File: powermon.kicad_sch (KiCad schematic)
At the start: 3 parts

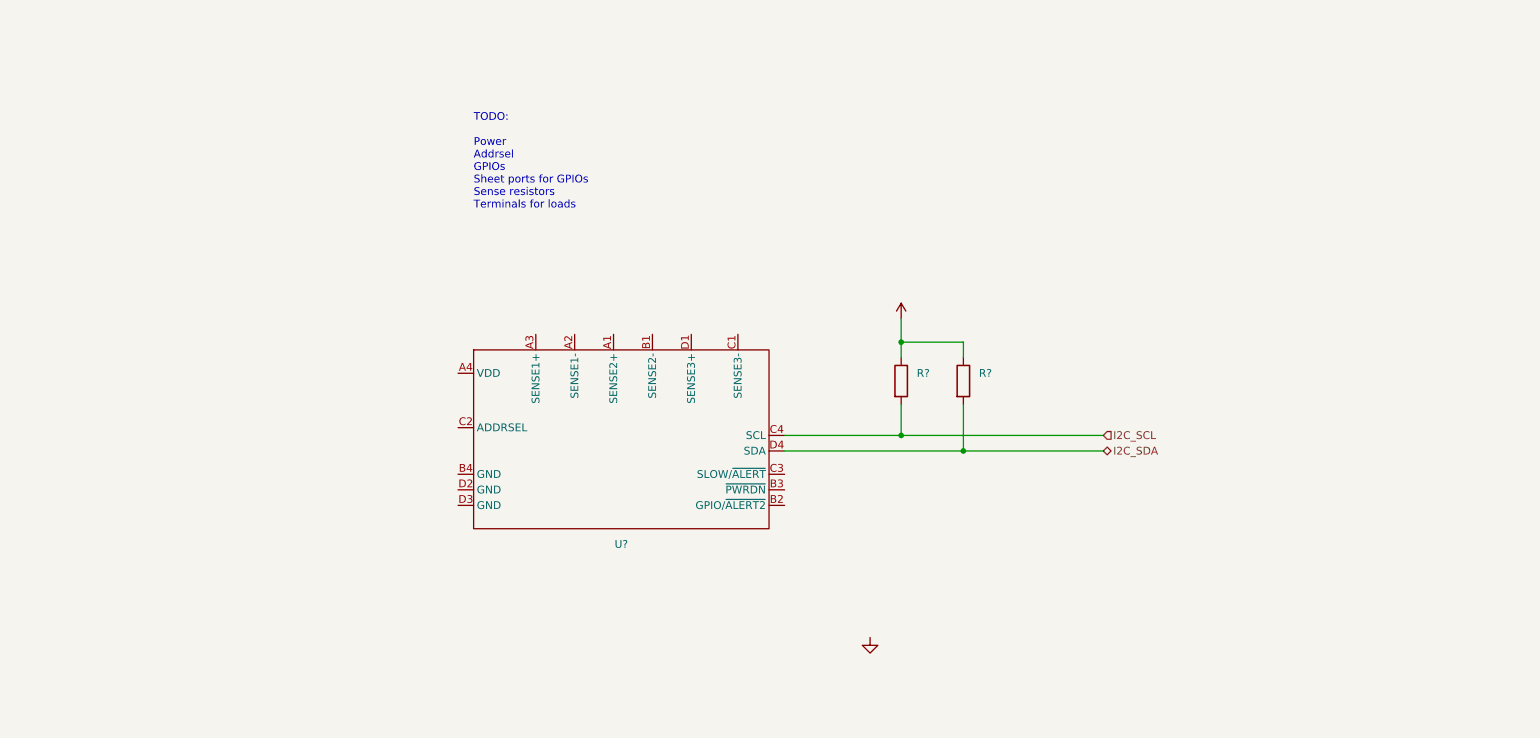
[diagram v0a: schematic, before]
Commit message: WiP: PAC1953 power monitor
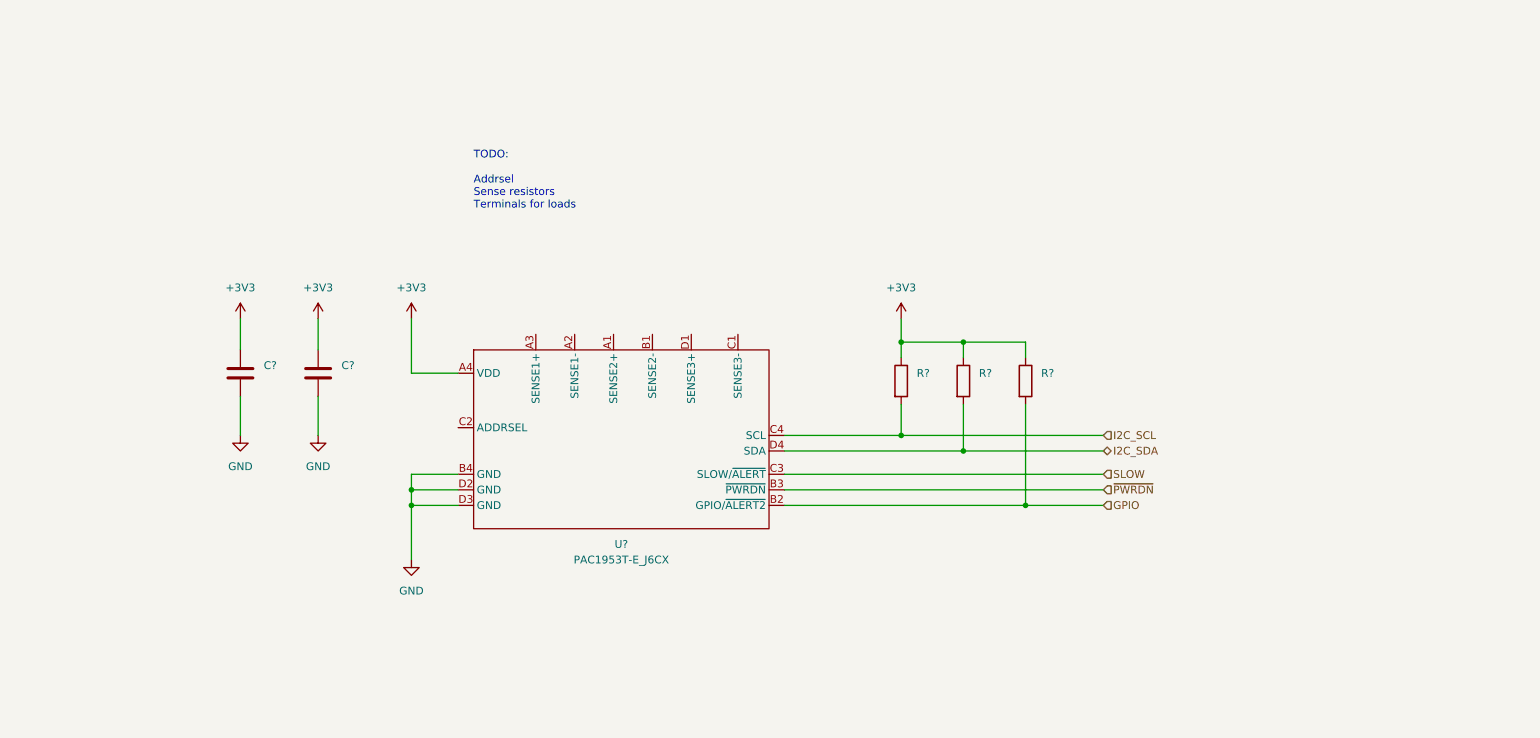
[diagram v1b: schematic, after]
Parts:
- added C? (x2): (no value), symbol Device:C
- added R?: (no value), symbol Device:R
- U?: value (none) -> PAC1953T-E_J6CX
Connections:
- net +3V3: now also U?.A4 (VDD), C?.1, C?.1, R?.1
- net GND: now also U?.B4 (GND), U?.D2 (GND), U?.D3 (GND), C?.2, C?.2
- net GPIO: now reaches U?.B2 (GPIO/~{ALERT2})
- net GPIO: now also R?.2
- net ~{PWRDN}: now reaches U?.B3 (~{PWRDN})
- net SLOW: now reaches U?.C3 (SLOW/~{ALERT})
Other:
- note added: "TODO: Addrsel Sense resistors Terminals for loads"
- note removed: "TODO: Power Addrsel GPIOs Sheet ports for GPIOs Sense resistors Terminals for loads"

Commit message: WiP: PAC1953 addrsel
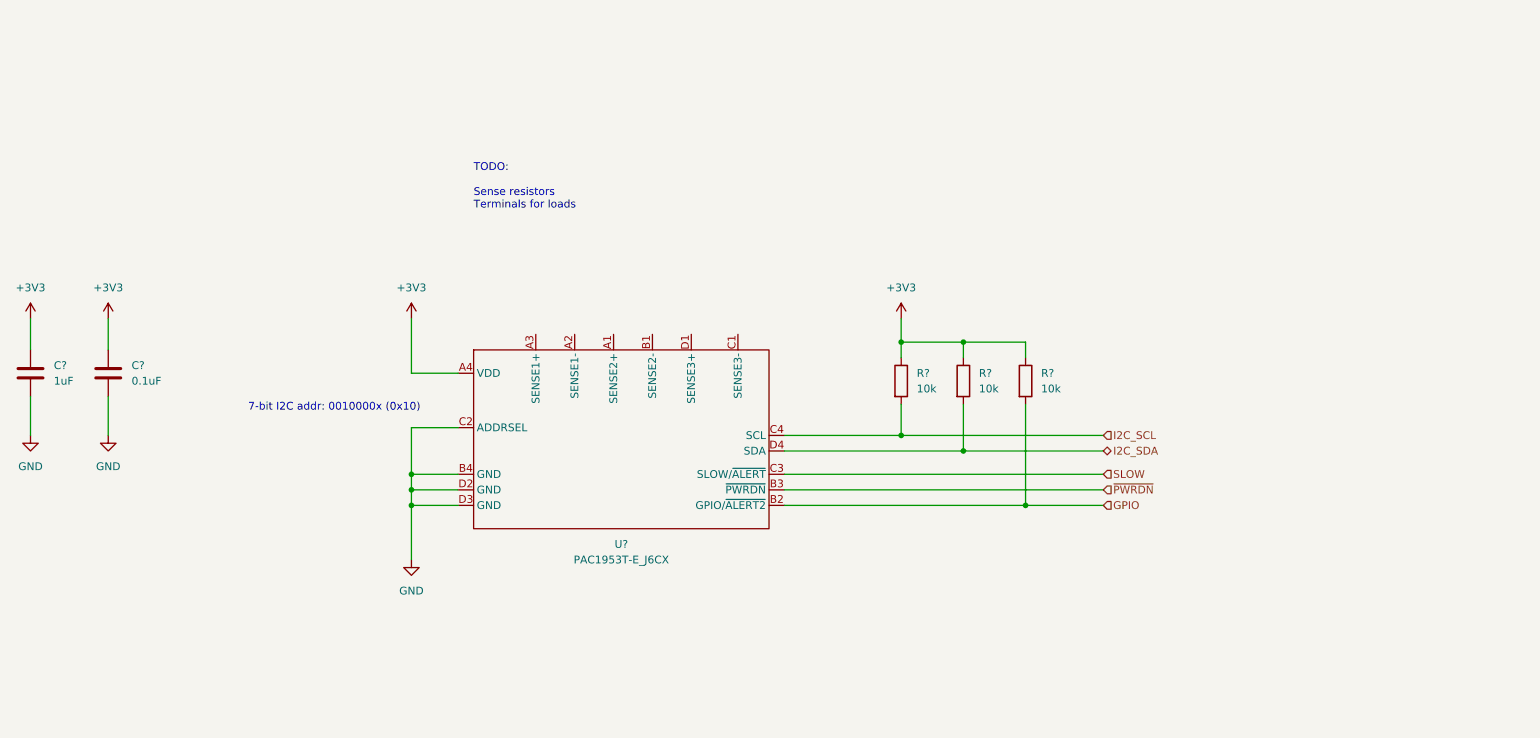
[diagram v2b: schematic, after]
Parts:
- C?: value (none) -> 1uF
- C?: value (none) -> 0.1uF
- R? (x3): value (none) -> 10k
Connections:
- net GND: now also U?.C2 (ADDRSEL)
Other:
- note added: "7-bit I2C addr: 0010000x (0x10)"
- note added: "TODO: Sense resistors Terminals for loads"
- note removed: "TODO: Addrsel Sense resistors Terminals for loads"
- moved on the sheet: C?
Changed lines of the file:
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@@
   (junction (at 189.23 91.44) (diameter 0) (color 0 0 0 0)
   )
+  (junction (at 109.22 113.03) (diameter 0) (color 0 0 0 0)
+  )
   (junction (at 199.39 109.22) (diameter 0) (color 0 0 0 0)
   )
-  (wire (pts (xy 93.98 87.63) (xy 93.98 92.71))
+  (wire (pts (xy 59.69 87.63) (xy 59.69 92.71))
     (stroke (width 0) (type default) (color 0 0 0 0))
   )
@@
     (stroke (width 0) (type default) (color 0 0 0 0))
   )
+  (wire (pts (xy 116.84 105.41) (xy 109.22 105.41))
+    (stroke (width 0) (type default) (color 0 0 0 0))
+  )
+  (wire (pts (xy 109.22 105.41) (xy 109.22 113.03))
+    (stroke (width 0) (type default) (color 0 0 0 0))
+  )
   (wire (pts (xy 199.39 101.6) (xy 199.39 109.22))
     (stroke (width 0) (type default) (color 0 0 0 0))
@@
     (stroke (width 0) (type default) (color 0 0 0 0))
   )
-  (wire (pts (xy 81.28 100.33) (xy 81.28 106.68))
+  (wire (pts (xy 46.99 100.33) (xy 46.99 106.68))
     (stroke (width 0) (type default) (color 0 0 0 0))
   )
@@
     (stroke (width 0) (type default) (color 0 0 0 0))
   )
-  (wire (pts (xy 81.28 87.63) (xy 81.28 92.71))
+  (wire (pts (xy 46.99 87.63) (xy 46.99 92.71))
     (stroke (width 0) (type default) (color 0 0 0 0))
   )
@@
     (stroke (width 0) (type default) (color 0 0 0 0))
   )
-  (wire (pts (xy 93.98 100.33) (xy 93.98 106.68))
+  (wire (pts (xy 59.69 100.33) (xy 59.69 106.68))
     (stroke (width 0) (type default) (color 0 0 0 0))
   )
@@
     (stroke (width 0) (type default) (color 0 0 0 0))
   )
-  (text "TODO:\n\nAddrsel\nSense resistors\nTerminals for loads"
-    (at 119.38 69.85 0)
+  (text "7-bit I2C addr: 0010000x (0x10)" (at 82.55 102.87 0)
     (effects (font (size 1.27 1.27)) (justify left bottom))
   )
+  (text "TODO:\n\nSense resistors\nTerminals for loads" (at 119.38 69.85 0)
+    (effects (font (size 1.27 1.27)) (justify left bottom))
+  )
   (hierarchical_label "I2C_SCL" (shape input) (at 222.25 106.68 0)
     (effects (font (size 1.27 1.27)) (justify left))
@@
       (effects (font (size 1.27 1.27)) (justify left))
     )
-    (property "Value" "" (id 1) (at 201.93 99.0599 0)
+    (property "Value" "10k" (id 1) (at 201.93 99.0599 0)
       (effects (font (size 1.27 1.27)) (justify left))
     )
@@
       (effects (font (size 1.27 1.27)) (justify left))
     )
-    (property "Value" "" (id 1) (at 191.77 99.0599 0)
+    (property "Value" "10k" (id 1) (at 191.77 99.0599 0)
       (effects (font (size 1.27 1.27)) (justify left))
     )
@@
     (pin "2")
   )
-  (symbol (lib_id "power:+3V3") (at 81.28 87.63 0) (unit 1)
-    (in_bom yes) (on_board yes) (fields_autoplaced)
-    (property "Reference" "#PWR?" (id 0) (at 81.28 91.44 0)
-      (effects (font (size 1.27 1.27)) hide)
-    )
-    (property "Value" "+3V3" (id 1) (at 81.28 82.55 0))
-    (property "Footprint" "" (id 2) (at 81.28 87.63 0)
-      (effects (font (size 1.27 1.27)) hide)
-    )
-    (property "Datasheet" "" (id 3) (at 81.28 87.63 0)
-      (effects (font (size 1.27 1.27)) hide)
-    )
-    (pin "1")
-  )
-  (symbol (lib_id "Device:C") (at 81.28 96.52 0) (unit 1)
-    (in_bom yes) (on_board yes) (fields_autoplaced)
-    (property "Reference" "C?" (id 0) (at 85.09 95.2499 0)
-      (effects (font (size 1.27 1.27)) (justify left))
-    )
-    (property "Value" "" (id 1) (at 85.09 97.7899 0)
-      (effects (font (size 1.27 1.27)) (justify left))
-    )
-    (property "Footprint" "" (id 2) (at 82.2452 100.33 0)
-      (effects (font (size 1.27 1.27)) hide)
-    )
-    (property "Datasheet" "~" (id 3) (at 81.28 96.52 0)
-      (effects (font (size 1.27 1.27)) hide)
-    )
-    (pin "1")
-    (pin "2")
-  )
-  (symbol (lib_id "power:GND") (at 93.98 106.68 0) (unit 1)
-    (in_bom yes) (on_board yes) (fields_autoplaced)
-    (property "Reference" "#PWR?" (id 0) (at 93.98 113.03 0)
-      (effects (font (size 1.27 1.27)) hide)
-    )
-    (property "Value" "GND" (id 1) (at 93.98 111.76 0))
-    (property "Footprint" "" (id 2) (at 93.98 106.68 0)
-      (effects (font (size 1.27 1.27)) hide)
-    )
-    (property "Datasheet" "" (id 3) (at 93.98 106.68 0)
+  (symbol (lib_id "power:+3V3") (at 46.99 87.63 0) (unit 1)
+    (in_bom yes) (on_board yes) (fields_autoplaced)
+    (property "Reference" "#PWR?" (id 0) (at 46.99 91.44 0)
+      (effects (font (size 1.27 1.27)) hide)
+    )
+    (property "Value" "+3V3" (id 1) (at 46.99 82.55 0))
+    (property "Footprint" "" (id 2) (at 46.99 87.63 0)
+      (effects (font (size 1.27 1.27)) hide)
+    )
+    (property "Datasheet" "" (id 3) (at 46.99 87.63 0)
+      (effects (font (size 1.27 1.27)) hide)
+    )
+    (pin "1")
+  )
+  (symbol (lib_id "Device:C") (at 46.99 96.52 0) (unit 1)
+    (in_bom yes) (on_board yes) (fields_autoplaced)
+    (property "Reference" "C?" (id 0) (at 50.8 95.2499 0)
+      (effects (font (size 1.27 1.27)) (justify left))
+    )
+    (property "Value" "1uF" (id 1) (at 50.8 97.7899 0)
+      (effects (font (size 1.27 1.27)) (justify left))
+    )
+    (property "Footprint" "" (id 2) (at 47.9552 100.33 0)
+      (effects (font (size 1.27 1.27)) hide)
+    )
+    (property "Datasheet" "~" (id 3) (at 46.99 96.52 0)
+      (effects (font (size 1.27 1.27)) hide)
+    )
+    (pin "1")
+    (pin "2")
+  )
+  (symbol (lib_id "power:GND") (at 59.69 106.68 0) (unit 1)
+    (in_bom yes) (on_board yes) (fields_autoplaced)
+    (property "Reference" "#PWR?" (id 0) (at 59.69 113.03 0)
+      (effects (font (size 1.27 1.27)) hide)
+    )
+    (property "Value" "GND" (id 1) (at 59.69 111.76 0))
+    (property "Footprint" "" (id 2) (at 59.69 106.68 0)
+      (effects (font (size 1.27 1.27)) hide)
+    )
+    (property "Datasheet" "" (id 3) (at 59.69 106.68 0)
       (effects (font (size 1.27 1.27)) hide)
     )
@@
     (pin "1")
   )
-  (symbol (lib_id "power:+3V3") (at 93.98 87.63 0) (unit 1)
-    (in_bom yes) (on_board yes) (fields_autoplaced)
-    (property "Reference" "#PWR?" (id 0) (at 93.98 91.44 0)
-      (effects (font (size 1.27 1.27)) hide)
-    )
-    (property "Value" "+3V3" (id 1) (at 93.98 82.55 0))
-    (property "Footprint" "" (id 2) (at 93.98 87.63 0)
-      (effects (font (size 1.27 1.27)) hide)
-    )
-    (property "Datasheet" "" (id 3) (at 93.98 87.63 0)
+  (symbol (lib_id "power:+3V3") (at 59.69 87.63 0) (unit 1)
+    (in_bom yes) (on_board yes) (fields_autoplaced)
+    (property "Reference" "#PWR?" (id 0) (at 59.69 91.44 0)
+      (effects (font (size 1.27 1.27)) hide)
+    )
+    (property "Value" "+3V3" (id 1) (at 59.69 82.55 0))
+    (property "Footprint" "" (id 2) (at 59.69 87.63 0)
+      (effects (font (size 1.27 1.27)) hide)
+    )
+    (property "Datasheet" "" (id 3) (at 59.69 87.63 0)
       (effects (font (size 1.27 1.27)) hide)
     )
@@
     (pin "1")
   )
-  (symbol (lib_id "Device:C") (at 93.98 96.52 0) (unit 1)
-    (in_bom yes) (on_board yes) (fields_autoplaced)
-    (property "Reference" "C?" (id 0) (at 97.79 95.2499 0)
-      (effects (font (size 1.27 1.27)) (justify left))
-    )
-    (property "Value" "" (id 1) (at 97.79 97.7899 0)
-      (effects (font (size 1.27 1.27)) (justify left))
-    )
-    (property "Footprint" "" (id 2) (at 94.9452 100.33 0)
-      (effects (font (size 1.27 1.27)) hide)
-    )
-    (property "Datasheet" "~" (id 3) (at 93.98 96.52 0)
-      (effects (font (size 1.27 1.27)) hide)
-    )
-    (pin "1")
-    (pin "2")
-  )
-  (symbol (lib_id "power:GND") (at 81.28 106.68 0) (unit 1)
-    (in_bom yes) (on_board yes) (fields_autoplaced)
-    (property "Reference" "#PWR?" (id 0) (at 81.28 113.03 0)
-      (effects (font (size 1.27 1.27)) hide)
-    )
-    (property "Value" "GND" (id 1) (at 81.28 111.76 0))
-    (property "Footprint" "" (id 2) (at 81.28 106.68 0)
-      (effects (font (size 1.27 1.27)) hide)
-    )
-    (property "Datasheet" "" (id 3) (at 81.28 106.68 0)
+  (symbol (lib_id "Device:C") (at 59.69 96.52 0) (unit 1)
+    (in_bom yes) (on_board yes) (fields_autoplaced)
+    (property "Reference" "C?" (id 0) (at 63.5 95.2499 0)
+      (effects (font (size 1.27 1.27)) (justify left))
+    )
+    (property "Value" "0.1uF" (id 1) (at 63.5 97.7899 0)
+      (effects (font (size 1.27 1.27)) (justify left))
+    )
+    (property "Footprint" "" (id 2) (at 60.6552 100.33 0)
+      (effects (font (size 1.27 1.27)) hide)
+    )
+    (property "Datasheet" "~" (id 3) (at 59.69 96.52 0)
+      (effects (font (size 1.27 1.27)) hide)
+    )
+    (pin "1")
+    (pin "2")
+  )
+  (symbol (lib_id "power:GND") (at 46.99 106.68 0) (unit 1)
+    (in_bom yes) (on_board yes) (fields_autoplaced)
+    (property "Reference" "#PWR?" (id 0) (at 46.99 113.03 0)
+      (effects (font (size 1.27 1.27)) hide)
+    )
+    (property "Value" "GND" (id 1) (at 46.99 111.76 0))
+    (property "Footprint" "" (id 2) (at 46.99 106.68 0)
+      (effects (font (size 1.27 1.27)) hide)
+    )
+    (property "Datasheet" "" (id 3) (at 46.99 106.68 0)
       (effects (font (size 1.27 1.27)) hide)
     )
@@
       (effects (font (size 1.27 1.27)) (justify left))
     )
-    (property "Value" "" (id 1) (at 212.09 99.0599 0)
-      (effects (font (size 1.27 1.27)) (justify left))
-    )
+    (property "Value" "10k" (id 1) (at 212.09 99.0599 0)
+      (effects (font (size 1.27 1.27)) (justify left))
+    )

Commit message: PAC1953 shunt resistors, terminals
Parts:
- added J? (x5): 2060-452/998-404, symbol Connector:Screw_Terminal_01x02
- added J?: (no value), symbol Connector:Screw_Terminal_01x02
- added R? (x3): (no value), symbol Device:R
- added TP? (x6): (no value), symbol Connector:TestPoint
- added TP? (x6): TP-PTH, symbol Connector:TestPoint
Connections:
- net GND: now also J?.2 (Pin_2), J?.2 (Pin_2), J?.2 (Pin_2), J?.2 (Pin_2), J?.2 (Pin_2), J?.2 (Pin_2), TP?.1, TP?.1, TP?.1, TP?.1, TP?.1, TP?.1
- net at U?.A1 (SENSE2+): now also J?.1 (Pin_1), R?.2, TP?.1
- net at U?.A2 (SENSE1-): now also J?.1 (Pin_1), R?.1, TP?.1
- net at U?.A3 (SENSE1+): now also J?.1 (Pin_1), R?.2, TP?.1
- net at U?.B1 (SENSE2-): now also R?.1, TP?.1
- net at U?.C1 (SENSE3-): now also J?.1 (Pin_1), R?.1, TP?.1
- net at U?.D1 (SENSE3+): now also J?.1 (Pin_1), R?.2, TP?.1
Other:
- note added: "1 A full scale"
- note added: "10 A full scale"
- note added: "100 mA full scale"
- note added: "Layout: Place PTH test points under terminal blocks (alt. for enclosure/panel-mount connectors)"
- note added: "Load"
- note added: "PA2512FKE7W0R01E: Rsense := 0.01 ohms Full Scale Current = 100 mV / Rsense = 10 A Pmax := 2 W Full Scale Power Dissipation = 1 W PE1206FRM7W0R1L: Rsense := 0.1 ohms, Pmax := 0.5 W FSC = 1 A, FSPD = 0.1 W RC1206FR-131RL: Rsense := 1 ohm, Pmax := 0.25 W FSC = 100 mA, FSPD = 0.01 W"
- note added: "Vsupply (0-32V)"
- note removed: "TODO: Sense resistors Terminals for loads"
- moved on the sheet: C?

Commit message: ERC
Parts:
- gave numbers to parts that had none: 27
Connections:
- net at R2.1, TP5.1, U1.B1 (SENSE2-): now also J5.1 (Pin_1)
